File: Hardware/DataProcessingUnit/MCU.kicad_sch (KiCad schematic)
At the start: 43 parts, among them J1 USB_B_Micro, J4 Conn_01x07, Q2 BC847, SW1 SW_Push, U3 STM32F103RBTx, Y1 32,768kHz /12.5p, Y2 8M

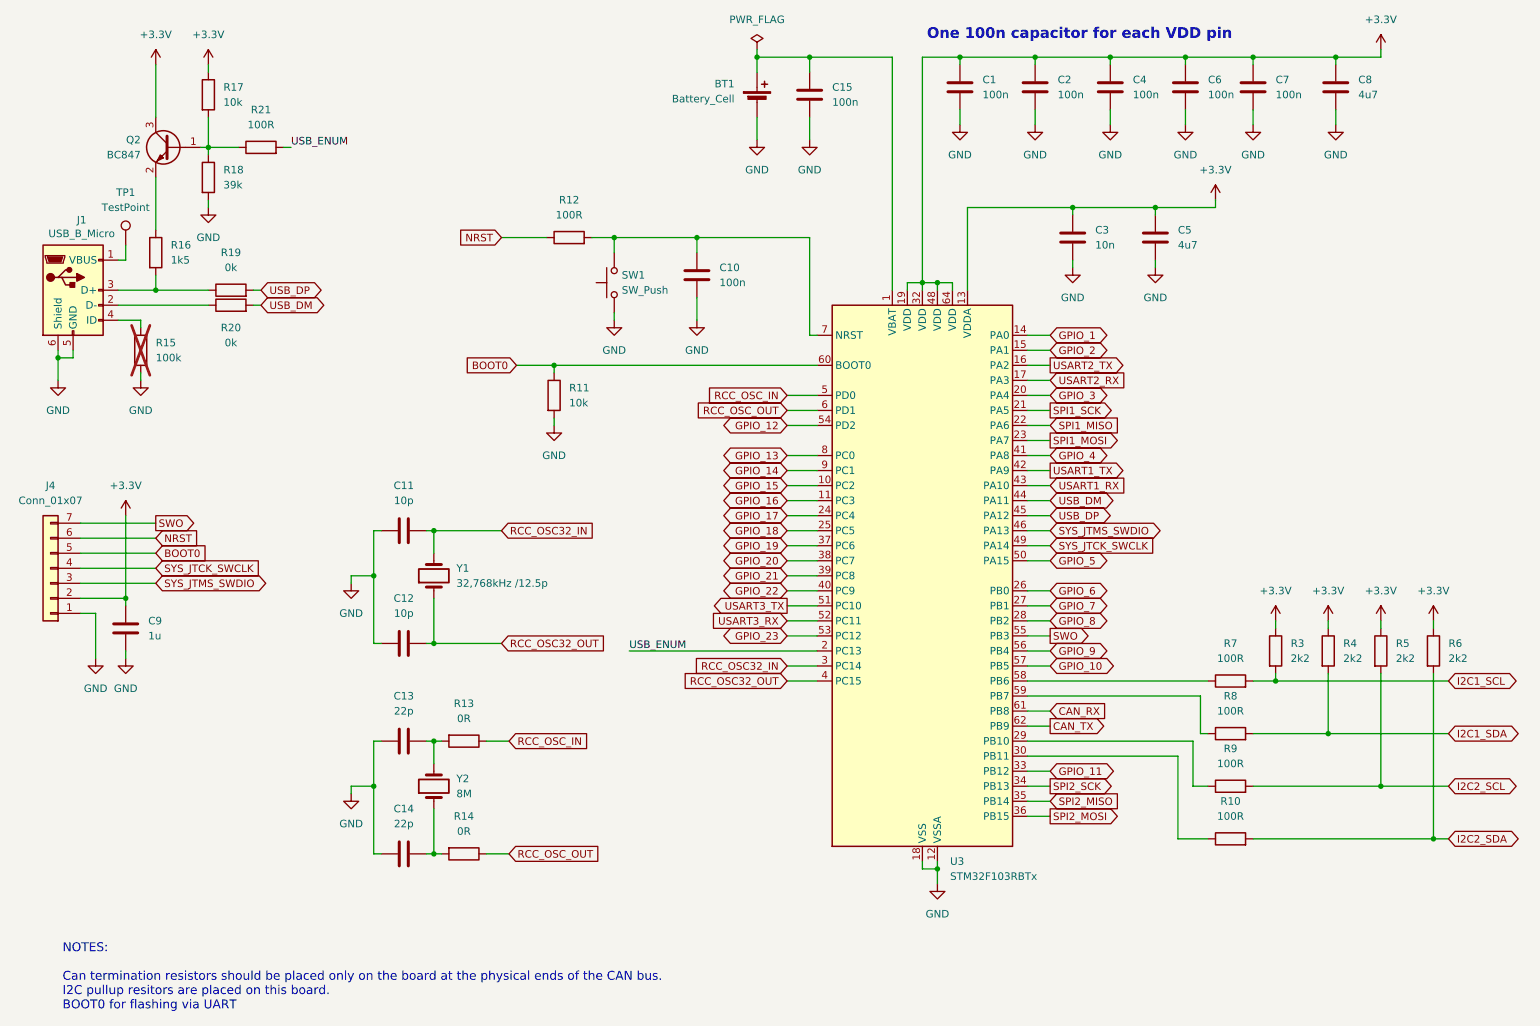
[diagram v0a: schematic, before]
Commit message: make boards smaller, fix sd card slot
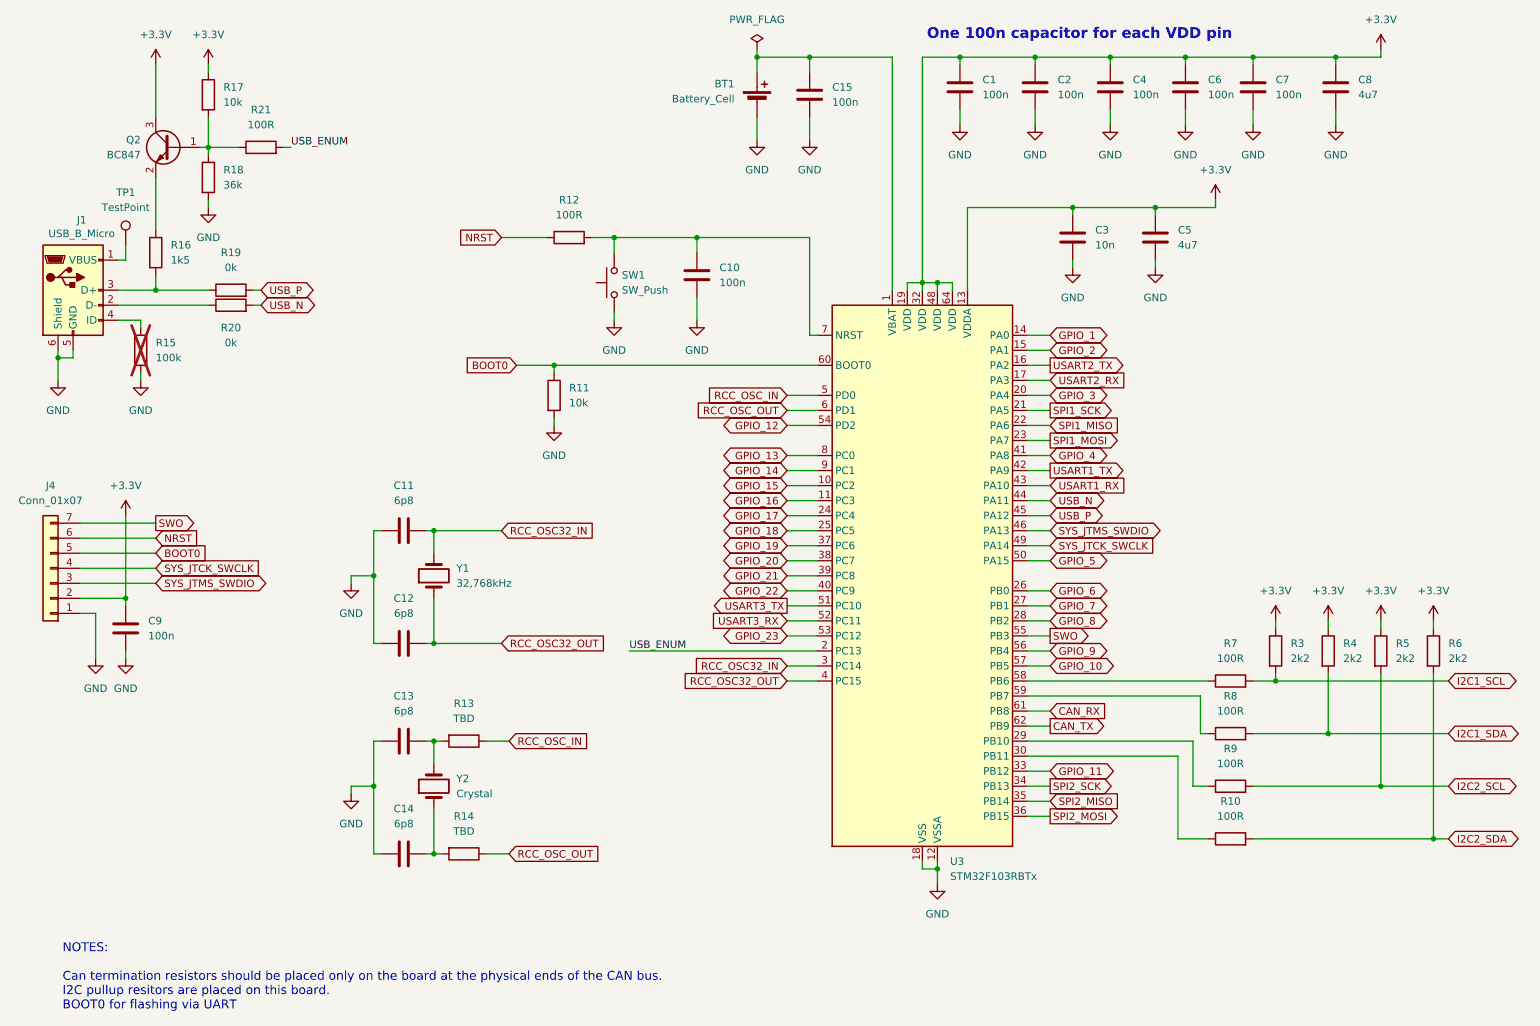
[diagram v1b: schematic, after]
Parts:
- C11, C12: value 10p -> 6p8
- C13, C14: value 22p -> 6p8
- C9: value 1u -> 100n
- R13, R14: value 0R -> TBD
- R18: value 39k -> 36k
- Y1: value 32,768kHz /12.5p -> 32,768kHz
- Y2: value 8M -> Crystal
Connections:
- net USB_DM renamed USB_N
- net USB_DP renamed USB_P
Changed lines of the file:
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@@
 		)
 	)
-	(global_label "USB_DM"
+	(global_label "USB_N"
 		(shape bidirectional)
 		(at 187.96 97.79 0)
@@
 		)
 		(property "Intersheetrefs" "${INTERSHEET_REFS}"
-			(at 199.5555 97.79 0)
+			(at 198.1646 97.79 0)
 			(effects
 				(font
@@
 		)
 	)
-	(global_label "USB_DP"
+	(global_label "USB_P"
 		(shape bidirectional)
 		(at 54.61 62.23 0)
@@
 		)
 		(property "Intersheetrefs" "${INTERSHEET_REFS}"
-			(at 66.0241 62.23 0)
+			(at 64.7541 62.23 0)
 			(effects
 				(font
@@
 		)
 	)
-	(global_label "USB_DM"
+	(global_label "USB_N"
 		(shape bidirectional)
 		(at 54.61 64.77 0)
@@
 		)
 		(property "Intersheetrefs" "${INTERSHEET_REFS}"
-			(at 66.2055 64.77 0)
+			(at 64.8146 64.77 0)
 			(effects
 				(font
@@
 		)
 	)
-	(global_label "USB_DP"
+	(global_label "USB_P"
 		(shape bidirectional)
 		(at 187.96 100.33 0)
@@
 		)
 		(property "Intersheetrefs" "${INTERSHEET_REFS}"
-			(at 199.3741 100.33 0)
+			(at 198.1041 100.33 0)
 			(effects
 				(font
@@
 			)
 		)
-		(property "Value" "8M"
+		(property "Value" "Crystal"
 			(at 87.63 147.3199 90)
 			(effects
@@
 			)
 		)
-		(property "Value" "10p"
+		(property "Value" "6p8"
 			(at 78.74 116.84 90)
 			(effects
@@
 			)
 		)
-		(property "Value" "32,768kHz /12.5p"
+		(property "Value" "32,768kHz"
 			(at 87.63 111.7599 90)
 			(effects
@@
 			)
 		)
-		(property "Value" "10p"
+		(property "Value" "6p8"
 			(at 78.74 97.79 90)
 			(effects
@@
 			)
 		)
-		(property "Value" "22p"
+		(property "Value" "6p8"
 			(at 78.74 152.4 90)
 			(effects
@@
 			)
 		)
-		(property "Value" "0R"
+		(property "Value" "TBD"
 			(at 88.9 134.62 90)
 			(effects
@@
 			)
 		)
-		(property "Value" "39k"
+		(property "Value" "36k"
 			(at 48.26 44.4499 0)
 			(effects
@@
 			)
 		)
-		(property "Value" "1u"
+		(property "Value" "100n"
 			(at 35.56 120.6499 0)
 			(effects
@@
 			)
 		)
-		(property "Value" "22p"
+		(property "Value" "6p8"
 			(at 78.74 133.35 90)
 			(effects
@@
 			)
 		)
-		(property "Value" "0R"
+		(property "Value" "TBD"
 			(at 88.9 153.67 90)
 			(effects

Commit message: xx
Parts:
- removed J1: USB_B_Micro, Connector_USB:USB_Micro-B_Molex-105017-0001, symbol Connector:USB_B_Micro
- added J2: USB_B_Micro, HardwareDataLogger:USB_Micro-B_Molex-105017-0001_Extra_Mechanical_Pads, symbol Connector:USB_B_Micro
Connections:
- net GND: now also J2.5 (GND), J2.6 (Shield)
- net at R20.1: now also J2.2 (D-)
- net at TP1.1: now also J2.1 (VBUS)
- net at R16.2, R19.1: now also J2.3 (D+)
- net at R15.1: now also J2.4 (ID)
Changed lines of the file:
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@@
-	)
-	(symbol
-		(lib_id "Connector:USB_B_Micro")
-		(at 22.86 62.23 0)
-		(unit 1)
-		(exclude_from_sim no)
-		(in_bom yes)
-		(on_board yes)
-		(dnp no)
-		(property "Reference" "J1"
-			(at 24.3078 50.3682 0)
-			(effects
-				(font
-					(size 1.27 1.27)
-				)
-			)
-		)
-		(property "Value" "USB_B_Micro"
-			(at 24.3078 52.6796 0)
-			(effects
-				(font
-					(size 1.27 1.27)
-				)
-			)
-		)
-		(property "Footprint" "Connector_USB:USB_Micro-B_Molex-105017-0001"
-			(at 26.67 63.5 0)
-			(effects
-				(font
-					(size 1.27 1.27)
-				)
-				(hide yes)
-			)
-		)
-		(property "Datasheet" "~"
-			(at 26.67 63.5 0)
-			(effects
-				(font
-					(size 1.27 1.27)
-				)
-				(hide yes)
-			)
-		)
-		(property "Description" ""
-			(at 22.86 62.23 0)
-			(effects
-				(font
-					(size 1.27 1.27)
-				)
-				(hide yes)
-			)
-		)
-		(pin "1"
-		)
-		(pin "2"
-		)
-		(pin "3"
-		)
-		(pin "4"
-		)
-		(pin "5"
-		)
-		(pin "6"
-		)
-		(instances
-			(project "DataProcessingUnit"
-				(path "/18f4643d-59cf-40d8-90af-99b4dbe1f32f/9bdfab82-cef8-460c-a16e-388f6d900e76"
-					(reference "J1")
-					(unit 1)
-				)
-			)
-		)
 	)
 	(symbol
@@
 					(unit 1)
 				)
+			)
+		)
+	)
+	(symbol
+		(lib_id "Connector:USB_B_Micro")
+		(at 22.86 62.23 0)
+		(unit 1)
+		(exclude_from_sim no)
+		(in_bom yes)
+		(on_board yes)
+		(dnp no)
+		(property "Reference" "J2"
+			(at 24.3078 50.3682 0)
+			(effects
+				(font
+					(size 1.27 1.27)
+				)
+			)
+		)
+		(property "Value" "USB_B_Micro"
+			(at 24.3078 52.6796 0)
+			(effects
+				(font
+					(size 1.27 1.27)
+				)
+			)
+		)
+		(property "Footprint" "HardwareDataLogger:USB_Micro-B_Molex-105017-0001_Extra_Mechanical_Pads"
+			(at 26.67 63.5 0)
+			(effects
+				(font
+					(size 1.27 1.27)
+				)
+				(hide yes)
+			)
+		)
+		(property "Datasheet" "~"
+			(at 26.67 63.5 0)
+			(effects
+				(font
+					(size 1.27 1.27)
+				)
+				(hide yes)
+			)
+		)
+		(property "Description" "USB Micro Type B connector"
+			(at 22.86 62.23 0)
+			(effects
+				(font
+					(size 1.27 1.27)
+				)
+				(hide yes)
+			)
+		)
+		(pin "1"
+		)
+		(pin "2"
+		)
+		(pin "3"
+		)
+		(pin "4"
+		)
+		(pin "5"
+		)
+		(pin "6"
+		)
+		(instances
+			(project "DataProcessingUnit"
+				(path "/18f4643d-59cf-40d8-90af-99b4dbe1f32f/9bdfab82-cef8-460c-a16e-388f6d900e76"
+					(reference "J2")
+					(unit 1)
+				)
